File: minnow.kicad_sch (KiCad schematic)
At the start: 68 parts, among them J3 PicoBlade, J3 USB_C_Receptacle_Host, J4 ARM_JTAG_SWD_10_Male, J4 VCCIO_EXT, P1 USB_C_Plug, SW1 SW_DIP_x04, U1 FT230XQ, U2 PI5A3157CEX, U3 PI5A3157CEX, U4 USB3740B-AI2, U5 SiP32432DR3

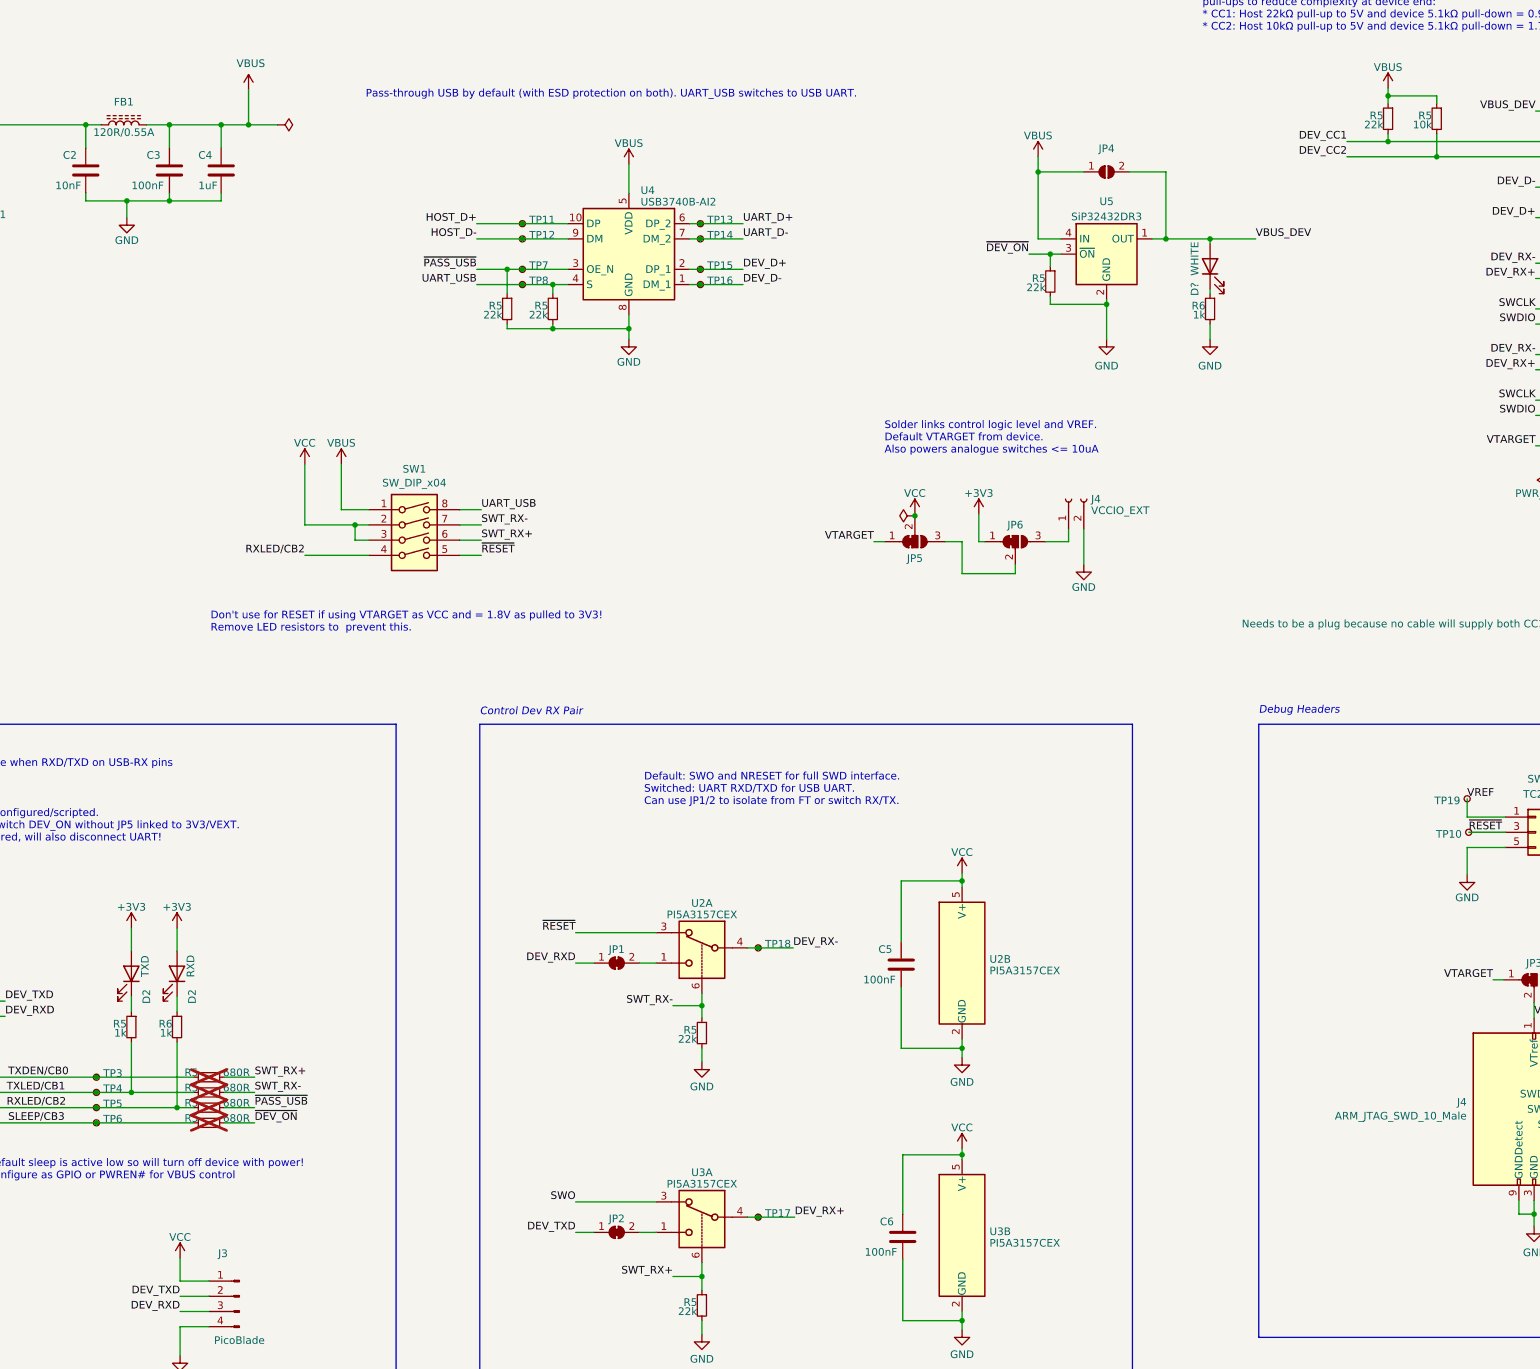
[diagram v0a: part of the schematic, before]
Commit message: Update Files
Update Files to KiCad 8.0
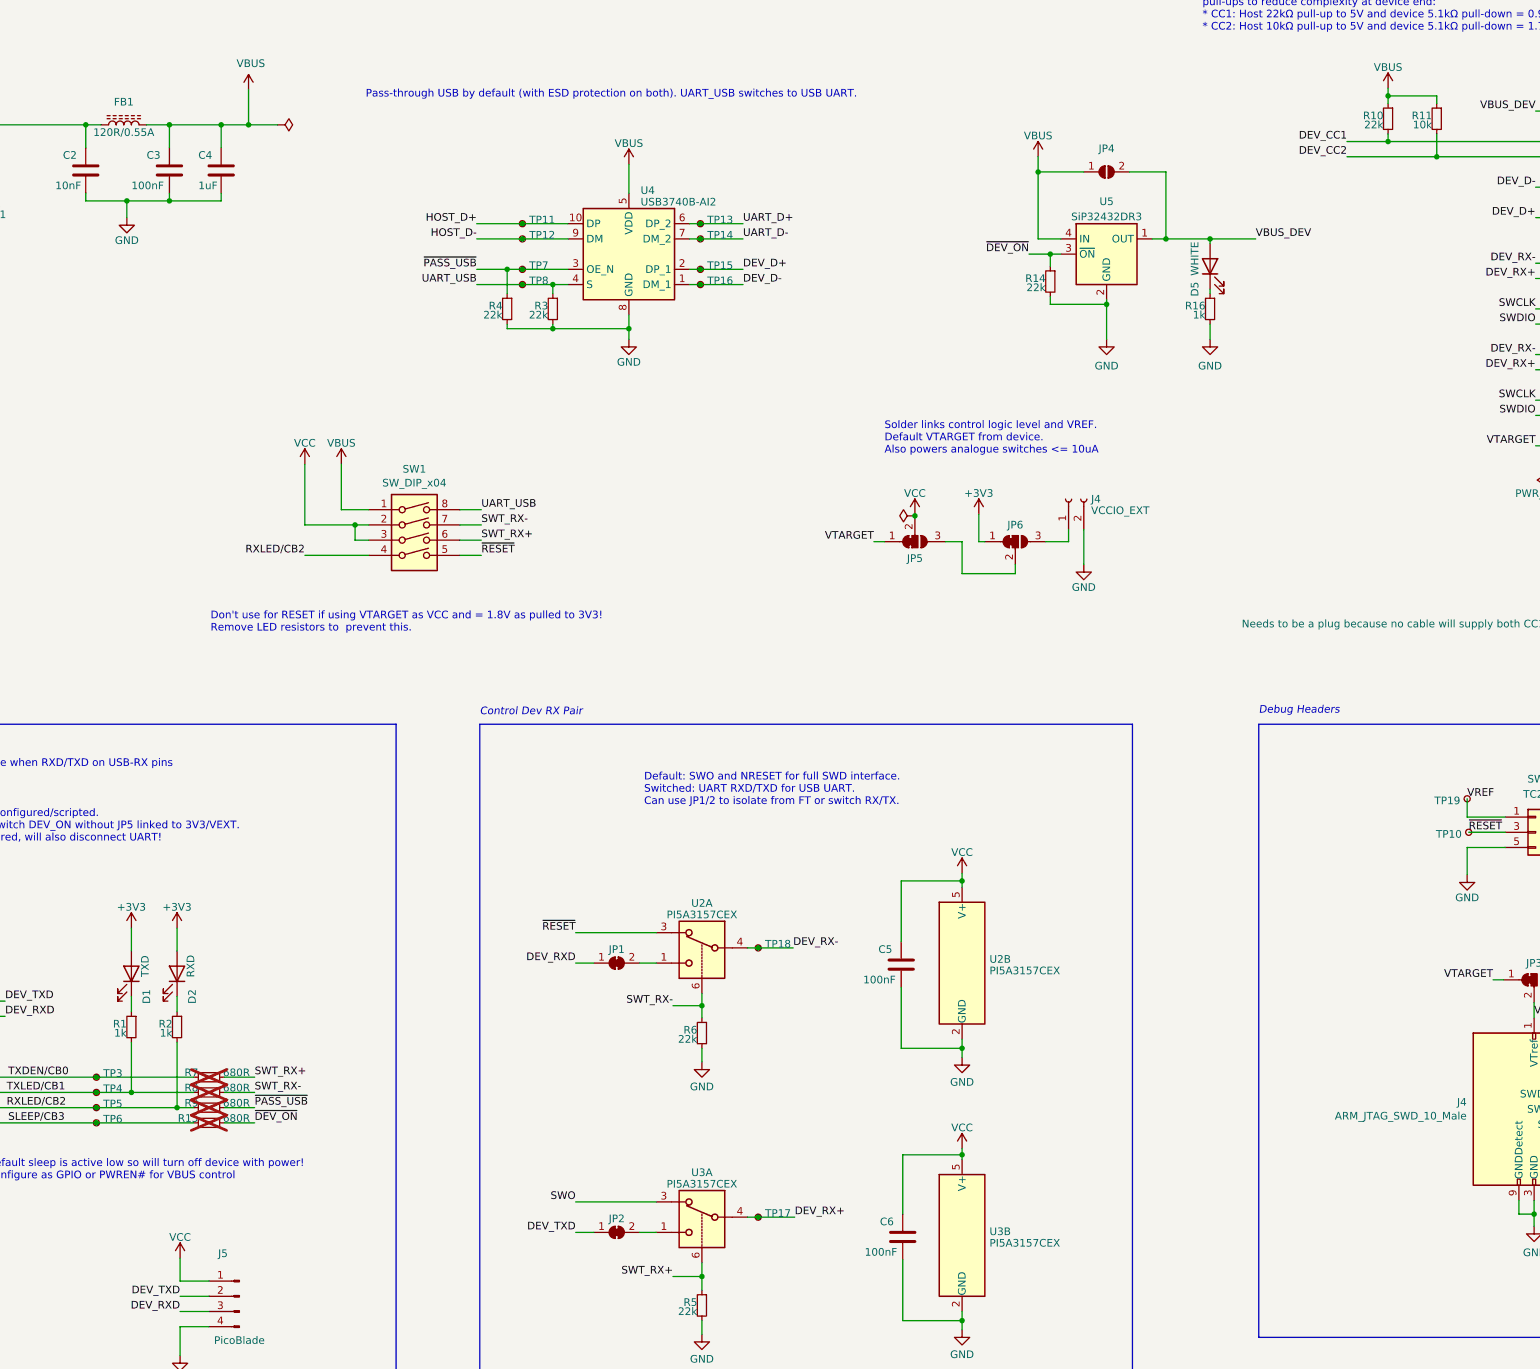
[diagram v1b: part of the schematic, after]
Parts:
- gave numbers to parts that had none: 1
- renumbered D2 to D1, J3 to J5, R5 to R1, R5 to R10, R5 to R11, R5 to R14, R5 to R15, R6 to R16, R6 to R2, R5 to R3, R5 to R4, R5 to R6, R5 to R7, R5 to R8, R5 to R9

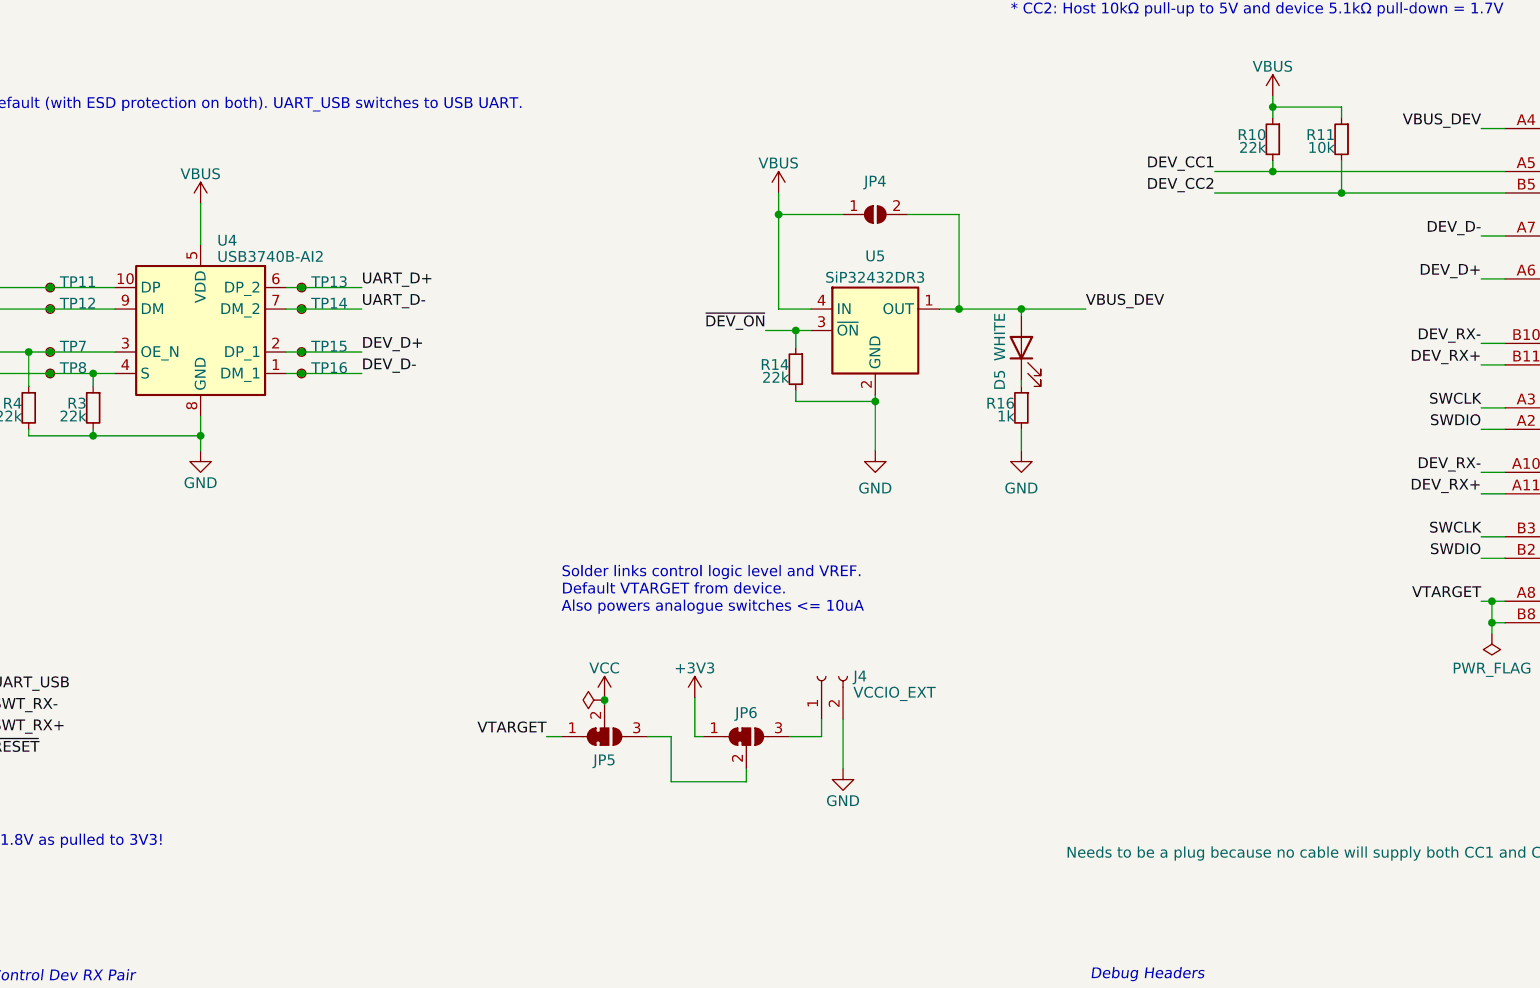
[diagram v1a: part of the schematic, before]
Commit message: Update minnow.kicad_sch
Add ESD diodes on output plug
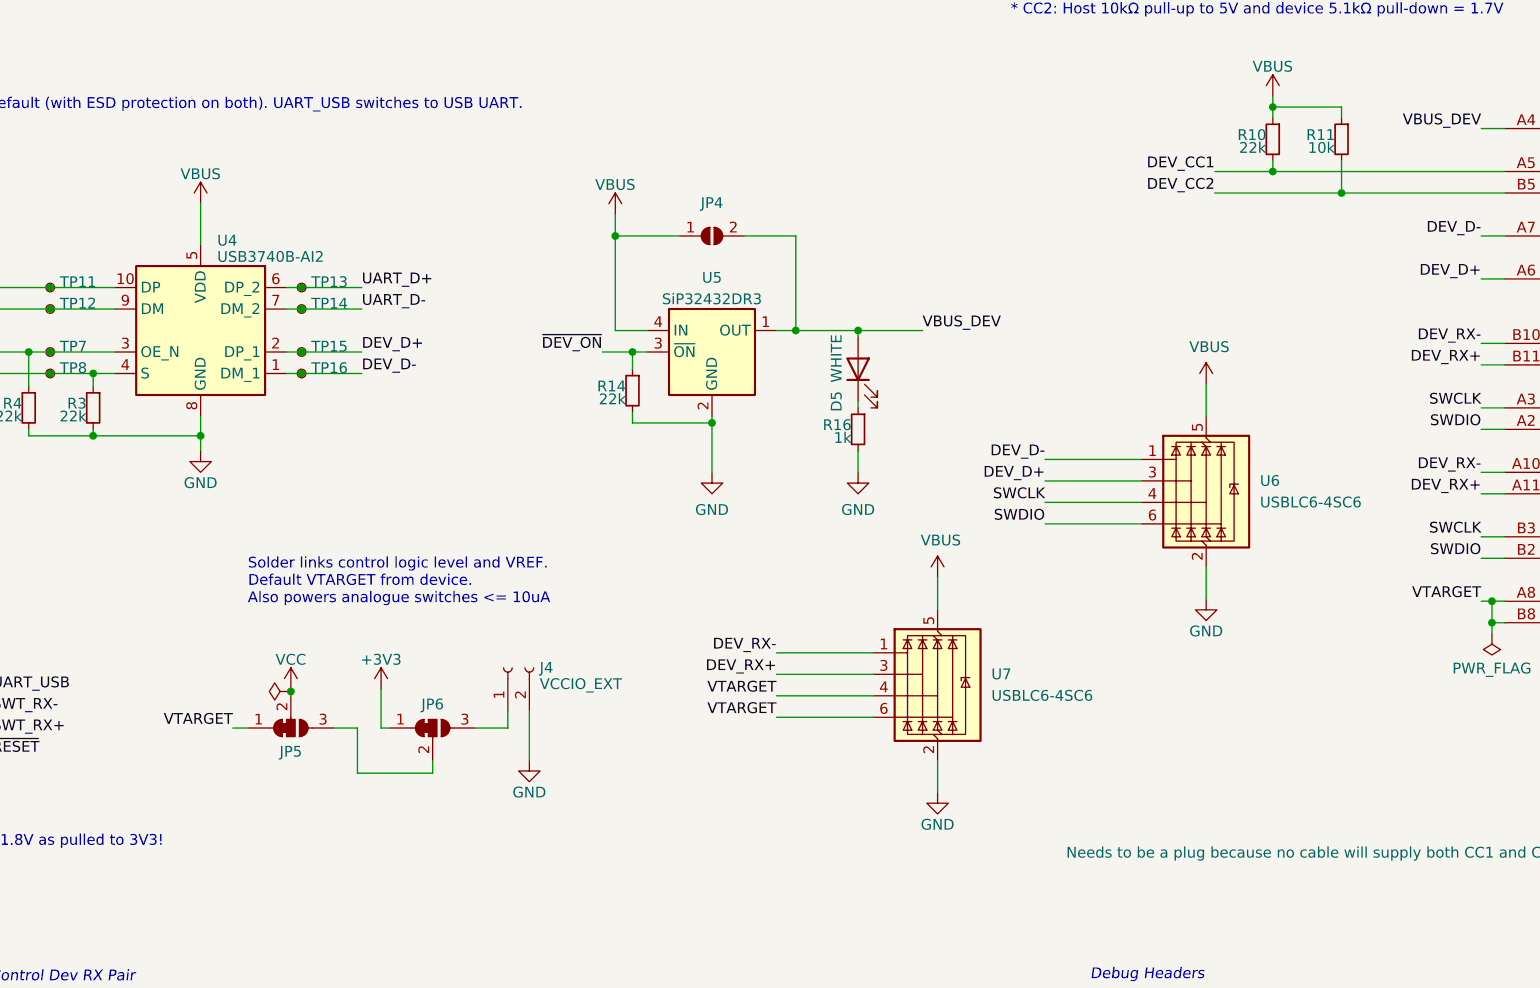
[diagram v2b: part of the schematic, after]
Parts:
- added U6, U7: USBLC6-4SC6, Package_TO_SOT_SMD:SOT-23-6, symbol Power_Protection:USBLC6-4SC6
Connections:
- net DEV_D+: now also U6.3 (I/O2)
- net DEV_D-: now also U6.1 (I/O1)
- net DEV_RX+: now also U7.3 (I/O2)
- net DEV_RX-: now also U7.1 (I/O1)
- net GND: now also U6.2 (GND), U7.2 (GND)
- net SWCLK: now also U6.4 (I/O3)
- net SWDIO: now also U6.6 (I/O4)
- net VBUS: now also U6.5 (VBUS), U7.5 (VBUS)
- net VTARGET: now also U7.4 (I/O3), U7.6 (I/O4)
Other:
- company: JBR Engineering Research Ltd -> (none)
- title: Minnow - USB-C DAM Tool -> DAMLink - USB-C DAM Tool
- moved on the sheet: D5, J4, JP4, JP5, JP6, R14, R16, U5
